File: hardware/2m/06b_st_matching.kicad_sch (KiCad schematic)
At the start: 19 parts

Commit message: Preserve M5B-E1 integrated RF2M evaluation baseline
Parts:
- C631: value 56p -> 22p; Engineering_Note ST nominal value; exact suffix/current stock and RF Q/volta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 -> M5B22p starting50ohm input match withL63447n/C63322p,includ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; MPN GRM1885C1H560JA01D -> GRM1885C1H220JA01D
- C633: value 27p -> 22p; Engineering_Note ST nominal value; exact suffix/current stock and RF Q/volta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 -> M5B22p initial50ohm input match,withC63122p/L63447n andreta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; MPN GRM1885C1H270JA01D -> GRM1885C1H220JA01D
- C635: Engineering_Note ST nominal value; exact suffix/current stock and RF Q/volta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 -> Murata1u25V X7R0603 local supply bypass;effective capacitan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; MPN OPEN: 1u rating/MPN -> GRM188R71E105KA12D
- L634: value 18n -> 47n; footprint (none) -> ARDF_2M:Coilcraft_0603HC_Doc218; Engineering_Note Original ST RF value/function. Exact manufacturer land/curr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 -> M5B50ohm initial match includes retainedL60633n bias-feed s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; MPN 0603HC-18NXJLU -> 0603HC-47NXJRW
- L635: footprint (none) -> ARDF_2M:Coilcraft_1812SMS_Doc184; Engineering_Note Final drain feed only: ST L3 nominal35.5nH conflicts with18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 -> RetainedST33nH feed;M5B exactDoc184-2 staggered land/curren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
- L638: footprint (none) -> ARDF_2M:Coilcraft_A05T_Doc107; Engineering_Note Original ST A05T nominal18.5nH. Coilcraft confirms5turns,Qm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 -> Actual Doc107-1 sizeA staggered lands,not generic axial pad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
- TL603: footprint (none) -> ARDF_2M:TL50_6p23mm; Engineering_Note Original ST0.508mm FR4,70umCu,W0.92mm,L6.23mm. Reference el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 -> M5B actual copper microstrip,0.8mm finished PCB/core0.64mm 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; now left out of the parts list
- TL604: footprint (none) -> ARDF_2M:TL50_6p62mm; Engineering_Note Original ST0.508mm FR4,70umCu,W0.92mm,L6.62mm. Reference el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 -> M5B actual copper microstrip,0.8mm finished PCB/core0.64mm 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; now left out of the parts list
- TL605: footprint (none) -> ARDF_2M:TL50_5p8mm; Engineering_Note Original ST0.508mm FR4,70umCu,W0.92mm,L5.8mm. Reference ele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 -> M5B actual copper microstrip,0.8mm finished PCB/core0.64mm 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; now left out of the parts list
- TL606: footprint (none) -> ARDF_2M:TL50_2p2mm; Engineering_Note Original ST0.508mm FR4,70umCu,W0.92mm,L2.2mm. Reference ele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 -> M5B actual copper microstrip,0.8mm finished PCB/core0.64mm 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; now left out of the parts list
- TL607: footprint (none) -> ARDF_2M:TL50_11p0mm; Engineering_Note Original ST0.508mm FR4,70umCu,W0.92mm,L11mm. Reference elec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 -> M5B actual copper microstrip,0.8mm finished PCB/core0.64mm 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; now left out of the parts list
- TL608: footprint (none) -> ARDF_2M:TL50_12p4mm; Engineering_Note Original ST0.508mm FR4,70umCu,W0.92mm,L12.4mm. Reference el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 -> M5B actual copper microstrip,0.8mm finished PCB/core0.64mm 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; now left out of the parts list
- TL609: footprint (none) -> ARDF_2M:TL50_2p0mm; Engineering_Note Original ST0.508mm FR4,70umCu,W0.92mm,L2mm. Reference elect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 -> M5B actual copper microstrip,0.8mm finished PCB/core0.64mm 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; now left out of the parts list
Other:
- note added: "M5B-E1: REVIEW / ALL hardware measurements NOT RUN / no ordering or manufacture."
- note removed: "M5A-R4: REVIEW / ALL hardware measurements NOT RUN / no ordering or manufacture."

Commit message: Implement M5B-E3 standard JLCPCB RF2M evaluation board
Recalculate and implement 1.6 mm / 1 oz RF geometry, power copper, thermal vias, connector holes and manufacturing legend. Preserve electrical functions and population variants. Add native-geometry DFM, regression checks and fresh native/fabrication review archives. CAD milestone only; no manufacturing or operational release.
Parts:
- C631, C632, C633, C634, C635, C636, C637, C638, C639: footprint Capacitor_SMD:C_0603_1608Metric -> ARDF_2M:C_0603_1608Metric_E3
- TL603: value 50R 6.23mm -> 50R 6.1129mm; footprint ARDF_2M:TL50_6p23mm -> ARDF_2M:TL50_E3_6p1129mm; Engineering_Note M5B actual copper microstrip,0.8mm finished PCB/core0.64mm 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 -> E3 recalculated50ohm microstrip on ordinary1.6mm/1oz FR4;no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
- TL604: value 50R 6.62mm -> 50R 6.4956mm; footprint ARDF_2M:TL50_6p62mm -> ARDF_2M:TL50_E3_6p4956mm; Engineering_Note M5B actual copper microstrip,0.8mm finished PCB/core0.64mm 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 -> E3 recalculated50ohm microstrip on ordinary1.6mm/1oz FR4;no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
- TL605: value 50R 5.8mm -> 50R 5.691mm; footprint ARDF_2M:TL50_5p8mm -> ARDF_2M:TL50_E3_5p691mm; Engineering_Note M5B actual copper microstrip,0.8mm finished PCB/core0.64mm 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 -> E3 recalculated50ohm microstrip on ordinary1.6mm/1oz FR4;no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
- TL606: value 50R 2.2mm -> 50R 2.1587mm; footprint ARDF_2M:TL50_2p2mm -> ARDF_2M:TL50_E3_2p1587mm; Engineering_Note M5B actual copper microstrip,0.8mm finished PCB/core0.64mm 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 -> E3 recalculated50ohm microstrip on ordinary1.6mm/1oz FR4;no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
- TL607: value 50R 11mm -> 50R 10.7933mm; footprint ARDF_2M:TL50_11p0mm -> ARDF_2M:TL50_E3_10p7933mm; Engineering_Note M5B actual copper microstrip,0.8mm finished PCB/core0.64mm 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 -> E3 recalculated50ohm microstrip on ordinary1.6mm/1oz FR4;no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
- TL608: value 50R 12.4mm -> 50R 12.167mm; footprint ARDF_2M:TL50_12p4mm -> ARDF_2M:TL50_E3_12p167mm; Engineering_Note M5B actual copper microstrip,0.8mm finished PCB/core0.64mm 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 -> E3 recalculated50ohm microstrip on ordinary1.6mm/1oz FR4;no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
- TL609: value 50R 2mm -> 50R 1.9624mm; footprint ARDF_2M:TL50_2p0mm -> ARDF_2M:TL50_E3_1p9624mm; Engineering_Note M5B actual copper microstrip,0.8mm finished PCB/core0.64mm 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 -> E3 recalculated50ohm microstrip on ordinary1.6mm/1oz FR4;no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
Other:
- note added: "M5B-E3: REVIEW / ALL hardware measurements NOT RUN / no ordering or manufacture."
- note removed: "M5B-E1: REVIEW / ALL hardware measurements NOT RUN / no ordering or manufacture."

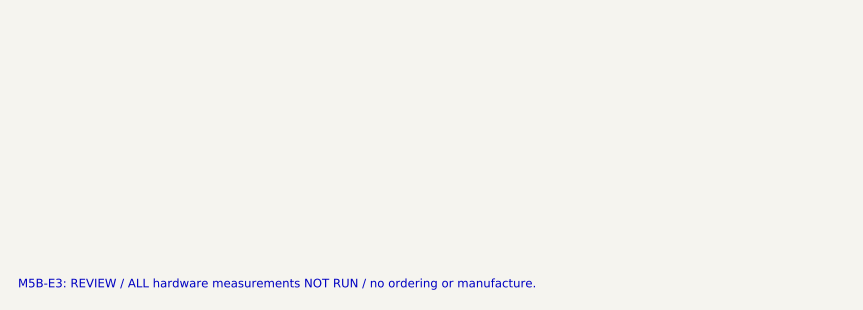
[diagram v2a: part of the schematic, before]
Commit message: Implement M5B-E4 thermal candidate with source-joint assembly hold
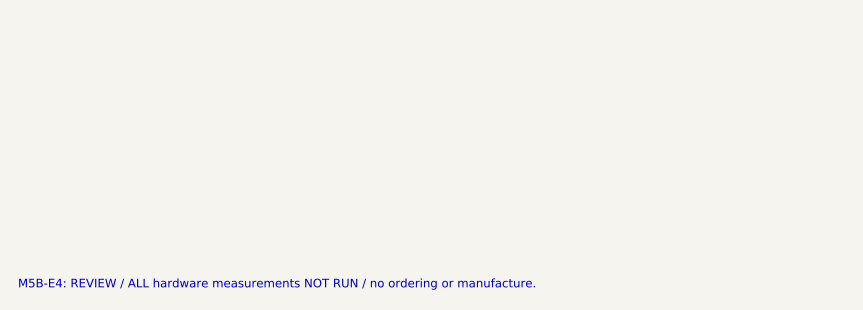
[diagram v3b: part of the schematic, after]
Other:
- note added: "M5B-E4: REVIEW / ALL hardware measurements NOT RUN / no ordering or manufacture."
- note removed: "M5B-E3: REVIEW / ALL hardware measurements NOT RUN / no ordering or manufacture."

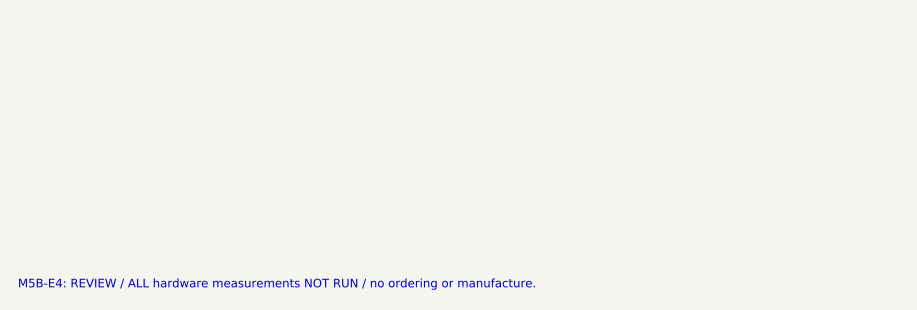
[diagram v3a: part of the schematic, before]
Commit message: Implement M5B-E4R1 source-joint prototype candidate
Replace source mask islands with a controlled open-via hybrid and native-derived local stencil. Preserve standard JLCPCB and RF circuitry. Add assembly qualification, thermal convergence and adverse sensitivities, native DFM/mutation checks and fresh review exports. Conservative 110 C target is missed; 125 C physical gate stays open. No acceptance tag or manufacturing authorization.
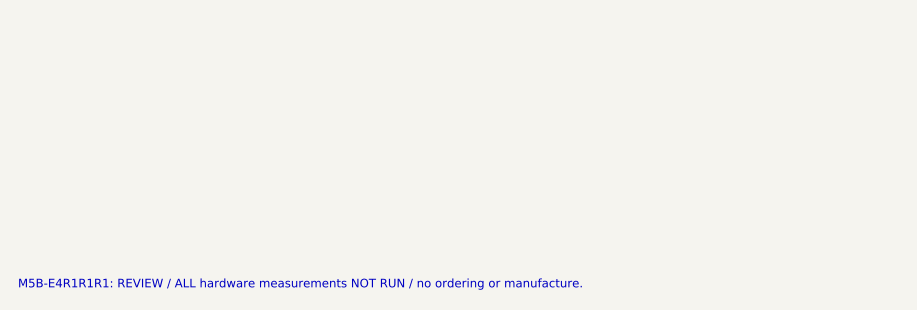
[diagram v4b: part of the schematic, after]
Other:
- note added: "M5B-E4R1R1R1: REVIEW / ALL hardware measurements NOT RUN / no ordering or manufacture."
- note removed: "M5B-E4: REVIEW / ALL hardware measurements NOT RUN / no ordering or manufacture."

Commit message: M5B-E5: compact RF2M to the shared 150x110 mm platform
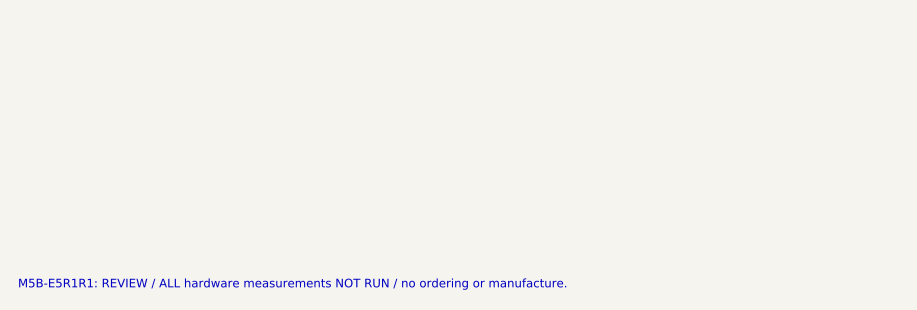
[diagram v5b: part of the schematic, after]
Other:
- note added: "M5B-E5R1R1: REVIEW / ALL hardware measurements NOT RUN / no ordering or manufacture."
- note removed: "M5B-E4R1R1R1: REVIEW / ALL hardware measurements NOT RUN / no ordering or manufacture."

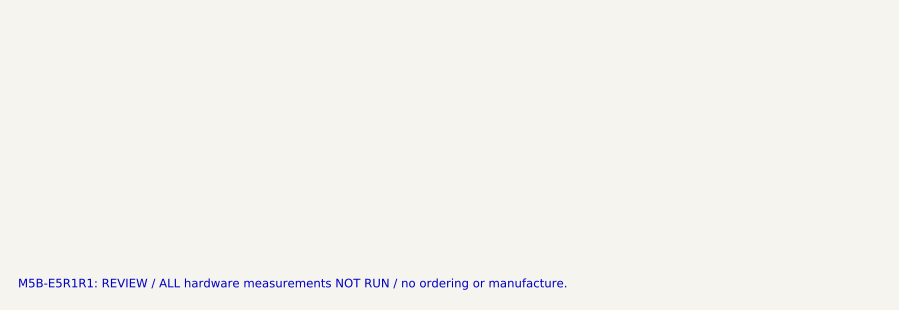
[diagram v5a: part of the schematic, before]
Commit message: M5B-E6R2: Implement carrier-keyed RF2M and unified cooling
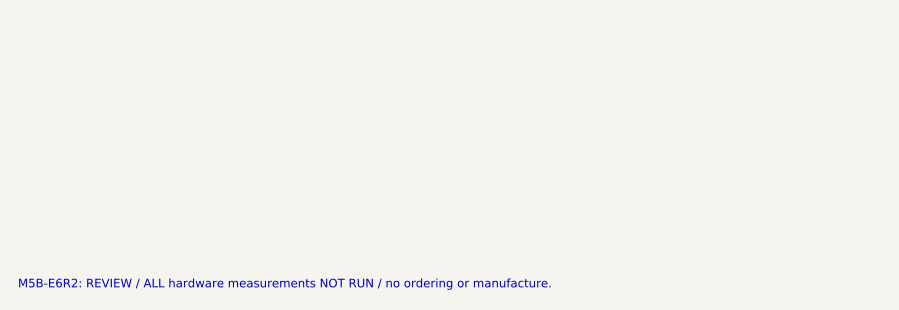
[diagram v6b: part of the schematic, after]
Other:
- note added: "M5B-E6R2: REVIEW / ALL hardware measurements NOT RUN / no ordering or manufacture."
- note removed: "M5B-E5R1R1: REVIEW / ALL hardware measurements NOT RUN / no ordering or manufacture."
